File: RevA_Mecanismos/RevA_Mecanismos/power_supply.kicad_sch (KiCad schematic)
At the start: 23 parts, among them Q1 NDS352AP, U2 R-78E3.3-1.0, U3 R-78E5.0-1.0

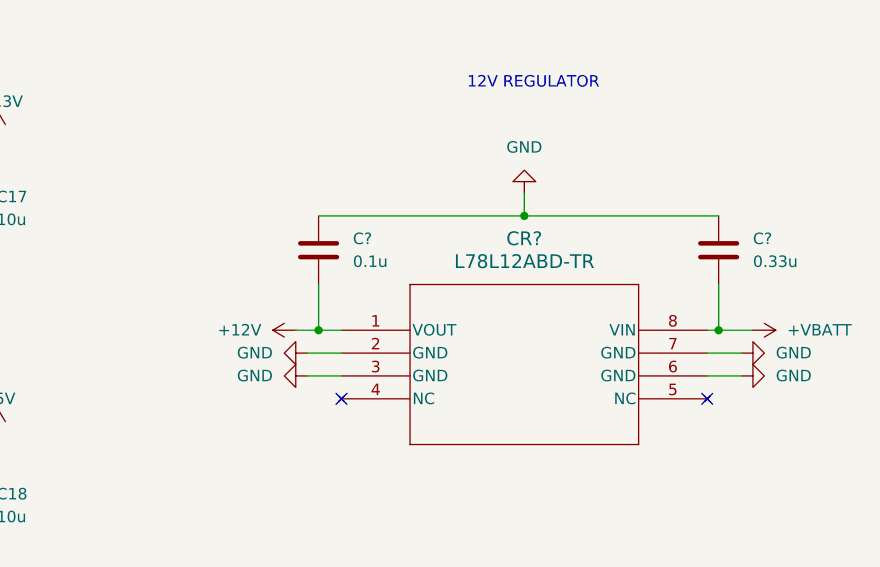
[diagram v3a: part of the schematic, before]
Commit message: Debug connectors and pwr flag to +12v
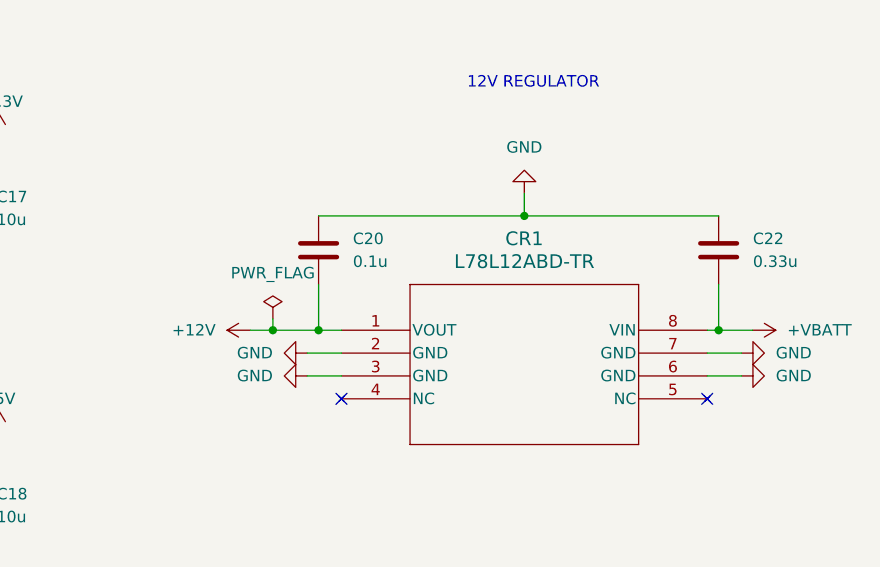
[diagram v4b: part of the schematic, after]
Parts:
- gave numbers to parts that had none: 3
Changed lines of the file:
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@@
   (junction (at 132.08 35.56) (diameter 0) (color 0 0 0 0)
   )
+  (junction (at 165.1 54.61) (diameter 0) (color 0 0 0 0)
+  )
+  (junction (at 170.18 54.61) (diameter 0) (color 0 0 0 0)
+  )
   (junction (at 54.61 173.99) (diameter 0) (color 0 0 0 0)
   )
@@
   )
   (junction (at 124.46 119.38) (diameter 0) (color 0 0 0 0)
-  )
-  (junction (at 170.18 54.61) (diameter 0) (color 0 0 0 0)
   )
   (junction (at 54.61 163.83) (diameter 0) (color 0 0 0 0)
@@
     (stroke (width 0) (type default))
   )
-  (wire (pts (xy 167.64 54.61) (xy 170.18 54.61))
-    (stroke (width 0) (type default))
-  )
   (wire (pts (xy 213.36 59.69) (xy 217.17 59.69))
     (stroke (width 0) (type default))
@@
   )
   (wire (pts (xy 118.11 78.74) (xy 132.08 78.74))
+    (stroke (width 0) (type default))
+  )
+  (wire (pts (xy 165.1 54.61) (xy 170.18 54.61))
     (stroke (width 0) (type default))
   )
@@
     (stroke (width 0) (type default))
   )
+  (wire (pts (xy 162.56 54.61) (xy 165.1 54.61))
+    (stroke (width 0) (type default))
+  )
   (wire (pts (xy 45.72 173.99) (xy 54.61 173.99))
+    (stroke (width 0) (type default))
+  )
+  (wire (pts (xy 165.1 53.34) (xy 165.1 54.61))
     (stroke (width 0) (type default))
   )
@@
   (symbol (lib_id "L78L12ABD-TR:L78L12ABD-TR") (at 172.72 54.61 0) (unit 1)
     (in_bom yes) (on_board yes) (dnp no) (fields_autoplaced)
-    (property "Reference" "CR?" (at 193.04 44.45 0)
+    (property "Reference" "CR1" (at 193.04 44.45 0)
       (effects (font (size 1.524 1.524)))
     )
@@
       (project "RevA_Mecanismos"
         (path "/3a16a434-10b7-49a8-988b-273362cb395e/9466c5e7-8595-42d4-852d-e47b24624149"
-          (reference "CR?") (unit 1)
+          (reference "CR1") (unit 1)
         )
       )
@@
     )
   )
-  (symbol (lib_id "power:+12V") (at 167.64 54.61 90) (unit 1)
-    (in_bom yes) (on_board yes) (dnp no) (fields_autoplaced)
-    (property "Reference" "#PWR094" (at 171.45 54.61 0)
-      (effects (font (size 1.27 1.27)) hide)
-    )
-    (property "Value" "+12V" (at 163.83 54.61 90)
-      (effects (font (size 1.27 1.27)) (justify left))
-    )
-    (property "Footprint" "" (at 167.64 54.61 0)
-      (effects (font (size 1.27 1.27)) hide)
-    )
-    (property "Datasheet" "" (at 167.64 54.61 0)
-      (effects (font (size 1.27 1.27)) hide)
-    )
-    (pin "1")
-    (instances
-      (project "RevA_Mecanismos"
-        (path "/3a16a434-10b7-49a8-988b-273362cb395e/9466c5e7-8595-42d4-852d-e47b24624149"
-          (reference "#PWR094") (unit 1)
-        )
-      )
-    )
-  )
   (symbol (lib_id "Device:C_Small") (at 104.14 40.64 180) (unit 1)
     (in_bom yes) (on_board yes) (dnp no) (fields_autoplaced)
@@
   (symbol (lib_id "Device:C") (at 214.63 45.72 0) (unit 1)
     (in_bom yes) (on_board yes) (dnp no) (fields_autoplaced)
-    (property "Reference" "C?" (at 218.44 44.45 0)
+    (property "Reference" "C22" (at 218.44 44.45 0)
       (effects (font (size 1.27 1.27)) (justify left))
     )
@@
       (project "RevA_Mecanismos"
         (path "/3a16a434-10b7-49a8-988b-273362cb395e/9466c5e7-8595-42d4-852d-e47b24624149"
-          (reference "C?") (unit 1)
+          (reference "C22") (unit 1)
         )
       )
@@
     )
   )
+  (symbol (lib_id "power:+12V") (at 162.56 54.61 90) (unit 1)
+    (in_bom yes) (on_board yes) (dnp no) (fields_autoplaced)
+    (property "Reference" "#PWR094" (at 166.37 54.61 0)
+      (effects (font (size 1.27 1.27)) hide)
+    )
+    (property "Value" "+12V" (at 158.75 54.61 90)
+      (effects (font (size 1.27 1.27)) (justify left))
+    )
+    (property "Footprint" "" (at 162.56 54.61 0)
+      (effects (font (size 1.27 1.27)) hide)
+    )
+    (property "Datasheet" "" (at 162.56 54.61 0)
+      (effects (font (size 1.27 1.27)) hide)
+    )
+    (pin "1")
+    (instances
+      (project "RevA_Mecanismos"
+        (path "/3a16a434-10b7-49a8-988b-273362cb395e/9466c5e7-8595-42d4-852d-e47b24624149"
+          (reference "#PWR094") (unit 1)
+        )
+      )
+    )
+  )
   (symbol (lib_id "Device:R") (at 54.61 168.91 0) (unit 1)
     (in_bom yes) (on_board yes) (dnp no) (fields_autoplaced)
@@
   (symbol (lib_id "Device:C") (at 170.18 45.72 0) (unit 1)
     (in_bom yes) (on_board yes) (dnp no) (fields_autoplaced)
-    (property "Reference" "C?" (at 173.99 44.45 0)
+    (property "Reference" "C20" (at 173.99 44.45 0)
       (effects (font (size 1.27 1.27)) (justify left))
     )
@@
       (project "RevA_Mecanismos"
         (path "/3a16a434-10b7-49a8-988b-273362cb395e/9466c5e7-8595-42d4-852d-e47b24624149"
-          (reference "C?") (unit 1)
+          (reference "C20") (unit 1)
         )
       )
@@
         )
       )
+    )
+  )
+  (symbol (lib_id "power:PWR_FLAG") (at 165.1 53.34 0) (unit 1)
+    (in_bom yes) (on_board yes) (dnp no) (fields_autoplaced)
+    (property "Reference" "#FLG06" (at 165.1 51.435 0)
+      (effects (font (size 1.27 1.27)) hide)
+    )
+    (property "Value" "PWR_FLAG" (at 165.1 48.26 0)
+      (effects (font (size 1.27 1.27)))
+    )
+    (property "Footprint" "" (at 165.1 53.34 0)
+      (effects (font (size 1.27 1.27)) hide)
+    )
+    (property "Datasheet" "~" (at 165.1 53.34 0)
+      (effects (font (size 1.27 1.27)) hide)
+    )
+    (pin "1")
+    (instances
+      (project "RevA_Mecanismos"
+        (path "/3a16a434-10b7-49a8-988b-273362cb395e/9466c5e7-8595-42d4-852d-e47b24624149"
+          (reference "#FLG06") (unit 1)
+        )
+      )

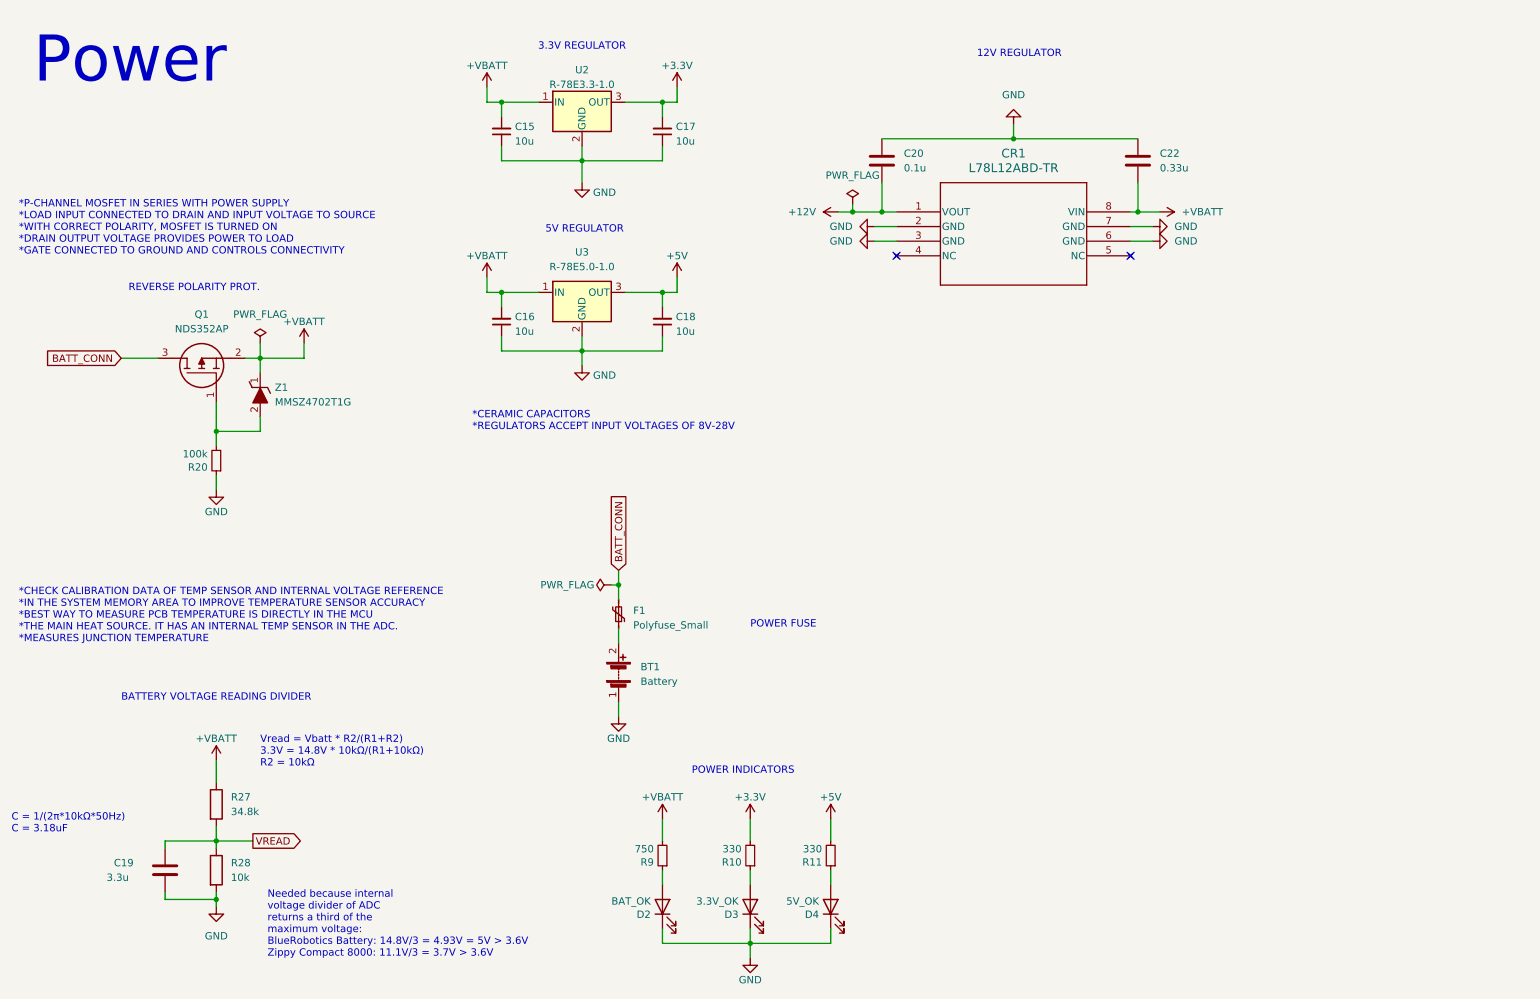
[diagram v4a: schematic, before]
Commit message: Updated STM32 USV Mechanism PCB
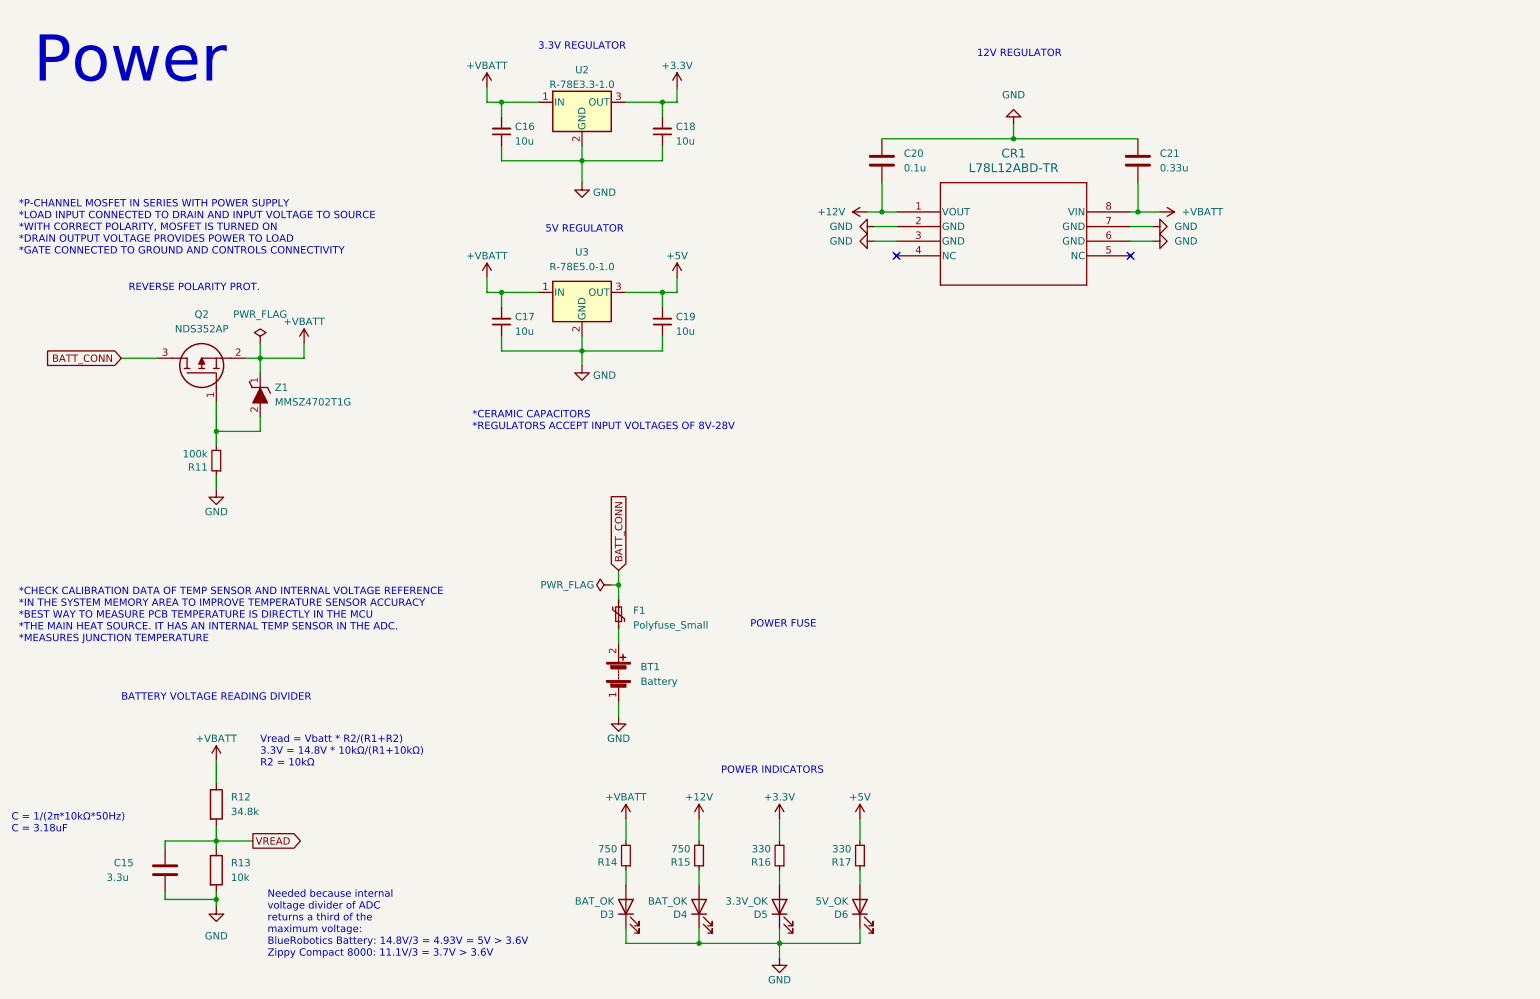
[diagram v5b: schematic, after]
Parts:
- removed R28: 10k, symbol Device:R
- added D4: BAT_OK, LED_SMD:LED_0603_1608Metric, symbol Device:LED
- added R13: 10k, Resistor_SMD:R_0603_1608Metric, symbol Device:R
- added R15: 750, Resistor_SMD:R_0603_1608Metric, symbol Device:R_Small
- C15: renamed from C19; footprint (none) -> Capacitor_SMD:C_0603_1608Metric
- C20: footprint (none) -> Capacitor_SMD:C_0603_1608Metric
- C21: renamed from C22; footprint (none) -> Capacitor_SMD:C_0603_1608Metric
- R12: renamed from R27; footprint (none) -> Resistor_SMD:R_0603_1608Metric
- renumbered C15 to C16, C16 to C17, C17 to C18, C18 to C19, D2 to D3, D3 to D5, D4 to D6, Q1 to Q2, R20 to R11, R9 to R14, R10 to R16, R11 to R17
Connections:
- net +12V: now also R15.2
- net GND: now also D4.1 (K), R13.2
- net VREAD: now also R13.1
- new net: D4.2 (A), R15.1
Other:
- moved on the sheet: D3, D5, D6, R14, R16, R17

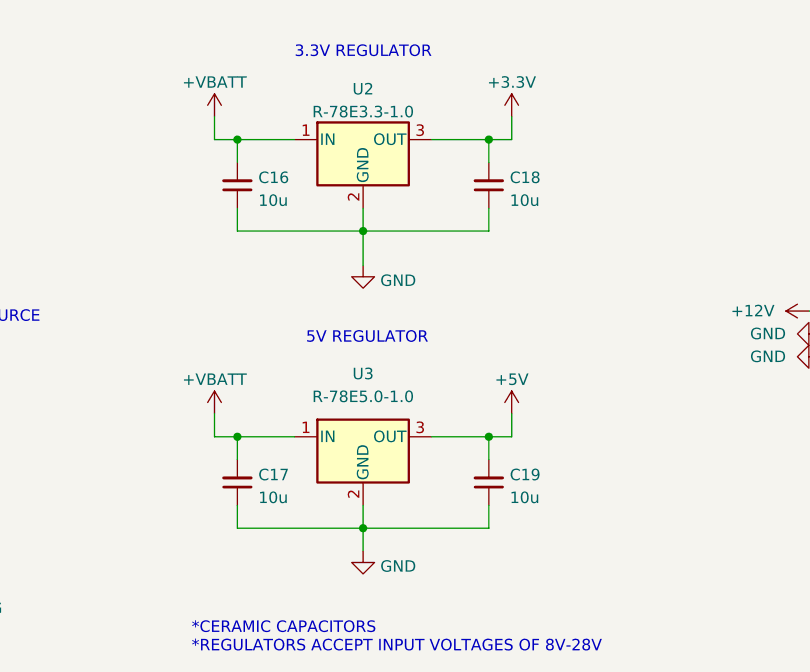
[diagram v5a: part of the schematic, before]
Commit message: Complete schematic and pcb designs, routes missing and not yet complete
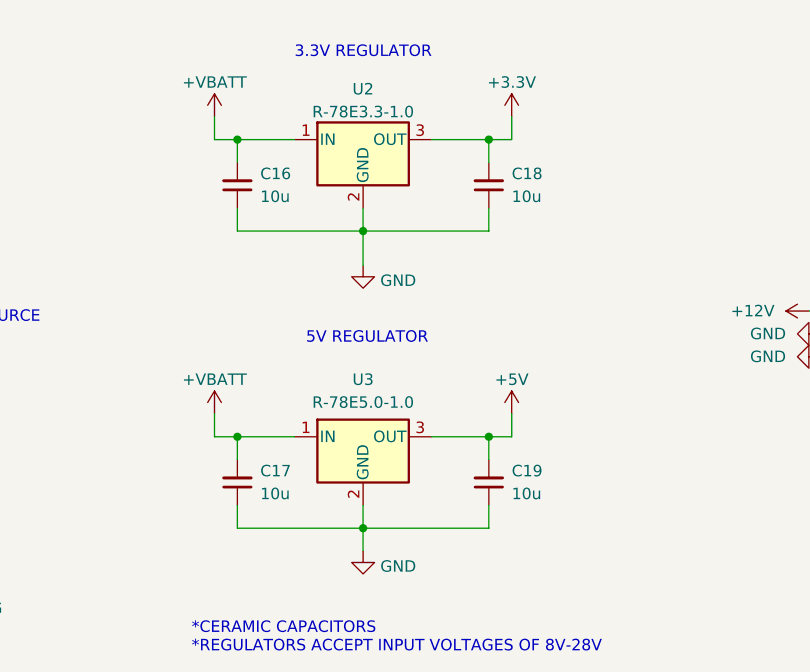
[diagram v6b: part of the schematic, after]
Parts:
- CR1: footprint SO-8_STM -> L78L12ABD-TR:SO-8_STM
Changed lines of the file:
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@@
       (effects (font (size 1.524 1.524)))
     )
-    (property "Footprint" "SO-8_STM" (at 172.72 54.61 0)
+    (property "Footprint" "L78L12ABD-TR:SO-8_STM" (at 172.72 54.61 0)
       (effects (font (size 1.27 1.27) italic) hide)
     )
@@
   (symbol (lib_id "Device:C_Small") (at 104.14 73.66 180) (unit 1)
     (in_bom yes) (on_board yes) (dnp no) (fields_autoplaced)
-    (property "Reference" "C17" (at 106.4641 72.8189 0)
-      (effects (font (size 1.27 1.27)) (justify right))
-    )
-    (property "Value" "10u" (at 106.4641 75.3558 0)
+    (property "Reference" "C17" (at 106.68 72.3836 0)
+      (effects (font (size 1.27 1.27)) (justify right))
+    )
+    (property "Value" "10u" (at 106.68 74.9236 0)
       (effects (font (size 1.27 1.27)) (justify right))
     )
@@
   (symbol (lib_id "Device:C_Small") (at 104.14 40.64 180) (unit 1)
     (in_bom yes) (on_board yes) (dnp no) (fields_autoplaced)
-    (property "Reference" "C16" (at 106.4641 39.7989 0)
-      (effects (font (size 1.27 1.27)) (justify right))
-    )
-    (property "Value" "10u" (at 106.4641 42.3358 0)
+    (property "Reference" "C16" (at 106.68 39.3636 0)
+      (effects (font (size 1.27 1.27)) (justify right))
+    )
+    (property "Value" "10u" (at 106.68 41.9036 0)
       (effects (font (size 1.27 1.27)) (justify right))
     )
@@
   (symbol (lib_id "Device:C_Small") (at 132.08 73.66 180) (unit 1)
     (in_bom yes) (on_board yes) (dnp no) (fields_autoplaced)
-    (property "Reference" "C19" (at 134.4041 72.8189 0)
-      (effects (font (size 1.27 1.27)) (justify right))
-    )
-    (property "Value" "10u" (at 134.4041 75.3558 0)
+    (property "Reference" "C19" (at 134.62 72.3836 0)
+      (effects (font (size 1.27 1.27)) (justify right))
+    )
+    (property "Value" "10u" (at 134.62 74.9236 0)
       (effects (font (size 1.27 1.27)) (justify right))
     )
@@
   (symbol (lib_id "Regulator_Switching:R-78E5.0-1.0") (at 118.11 68.58 0) (unit 1)
     (in_bom yes) (on_board yes) (dnp no) (fields_autoplaced)
-    (property "Reference" "U3" (at 118.11 61.595 0)
-      (effects (font (size 1.27 1.27)))
-    )
-    (property "Value" "R-78E5.0-1.0" (at 118.11 64.135 0)
+    (property "Reference" "U3" (at 118.11 62.23 0)
+      (effects (font (size 1.27 1.27)))
+    )
+    (property "Value" "R-78E5.0-1.0" (at 118.11 64.77 0)
       (effects (font (size 1.27 1.27)))
     )
@@
   (symbol (lib_id "Device:C_Small") (at 132.08 40.64 180) (unit 1)
     (in_bom yes) (on_board yes) (dnp no) (fields_autoplaced)
-    (property "Reference" "C18" (at 134.4041 39.7989 0)
-      (effects (font (size 1.27 1.27)) (justify right))
-    )
-    (property "Value" "10u" (at 134.4041 42.3358 0)
-      (effects (font (size 1.27 1.27)) (justify right))
-    )
+    (property "Reference" "C18" (at 134.62 39.3636 0)
+      (effects (font (size 1.27 1.27)) (justify right))
+    )
+    (property "Value" "10u" (at 134.62 41.9036 0)
+      (effects (font (size 1.27 1.27)) (justify right))
+    )
